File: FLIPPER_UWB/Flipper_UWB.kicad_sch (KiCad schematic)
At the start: 13 parts, among them IC1 DWM1000, J1 Conn_01x08_Socket, J2 Conn_01x10_Socket

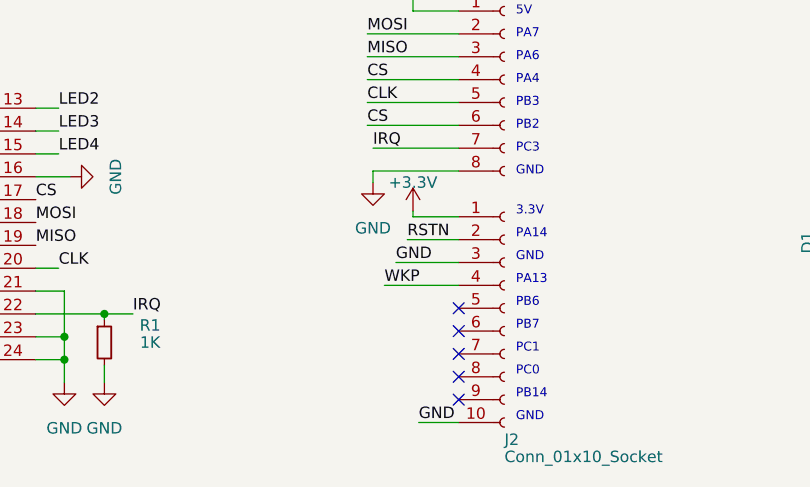
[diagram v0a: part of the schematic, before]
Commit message: Update and correction shield UWB
Update and correction of the Flipper Zero UWB shield.
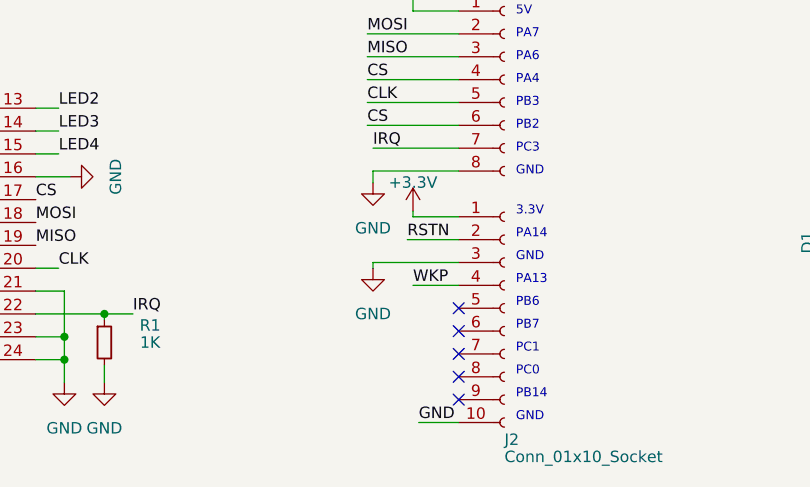
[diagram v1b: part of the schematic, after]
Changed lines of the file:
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@@
-    (stroke (width 0) (type default))
-  )
-  (wire (pts (xy 131.445 56.515) (xy 138.43 56.515))
     (stroke (width 0) (type default))
   )
@@
     (stroke (width 0) (type default))
   )
+  (wire (pts (xy 133.35 59.055) (xy 138.43 59.055))
+    (stroke (width 0) (type default))
+  )
   (wire (pts (xy 212.09 62.23) (xy 212.09 56.515))
     (stroke (width 0) (type default))
@@
     (stroke (width 0) (type default))
   )
+  (wire (pts (xy 128.905 56.515) (xy 138.43 56.515))
+    (stroke (width 0) (type default))
+  )
   (wire (pts (xy 133.35 51.435) (xy 133.35 50.8))
     (stroke (width 0) (type default))
@@
     (stroke (width 0) (type default))
   )
-  (wire (pts (xy 130.175 59.055) (xy 138.43 59.055))
-    (stroke (width 0) (type default))
-  )
   (wire (pts (xy 27.94 57.15) (xy 27.94 58.42))
     (stroke (width 0) (type default))
@@
     (stroke (width 0) (type default))
   )
+  (wire (pts (xy 128.905 56.515) (xy 128.905 57.15))
+    (stroke (width 0) (type default))
+  )
   (wire (pts (xy 21.59 54.61) (xy 33.02 54.61))
     (stroke (width 0) (type default))
@@
     (effects (font (size 1.27 1.27)) (justify left bottom))
   )
-  (label "WKP" (at 130.175 59.055 0) (fields_autoplaced)
+  (label "WKP" (at 133.35 59.055 0) (fields_autoplaced)
     (effects (font (size 1.27 1.27)) (justify left bottom))
   )
@@
     (effects (font (size 1.27 1.27)) (justify left bottom))
   )
-  (label "GND" (at 131.445 56.515 0) (fields_autoplaced)
-    (effects (font (size 1.27 1.27)) (justify left bottom))
-  )
   (label "LED4" (at 93.98 44.45 0) (fields_autoplaced)
     (effects (font (size 1.27 1.27)) (justify left bottom))
@@
     (pin "2")
     (instances
-      (project "Flipper"
+      (project "Flipper_UWB"
         (path "/250e14ef-3436-4bf2-8d4e-c0bb14da8bba"
           (reference "D3") (unit 1)
@@
     (pin "1")
     (instances
-      (project "Flipper"
+      (project "Flipper_UWB"
         (path "/250e14ef-3436-4bf2-8d4e-c0bb14da8bba"
           (reference "#PWR03") (unit 1)
@@
     (pin "2")
     (instances
-      (project "Flipper"
+      (project "Flipper_UWB"
         (path "/250e14ef-3436-4bf2-8d4e-c0bb14da8bba"
           (reference "D4") (unit 1)
@@
     (pin "1")
     (instances
-      (project "Flipper"
+      (project "Flipper_UWB"
         (path "/250e14ef-3436-4bf2-8d4e-c0bb14da8bba"
           (reference "#PWR05") (unit 1)
@@
     (pin "2")
     (instances
-      (project "Flipper"
+      (project "Flipper_UWB"
         (path "/250e14ef-3436-4bf2-8d4e-c0bb14da8bba"
           (reference "R1") (unit 1)
@@
     (pin "2")
     (instances
-      (project "Flipper"
+      (project "Flipper_UWB"
         (path "/250e14ef-3436-4bf2-8d4e-c0bb14da8bba"
           (reference "R2") (unit 1)
@@
     (pin "1")
     (instances
-      (project "Flipper"
+      (project "Flipper_UWB"
         (path "/250e14ef-3436-4bf2-8d4e-c0bb14da8bba"
           (reference "#PWR06") (unit 1)
@@
     (pin "8")
     (instances
-      (project "Flipper"
+      (project "Flipper_UWB"
         (path "/250e14ef-3436-4bf2-8d4e-c0bb14da8bba"
           (reference "J1") (unit 1)
@@
     (pin "1")
     (instances
-      (project "Flipper"
+      (project "Flipper_UWB"
         (path "/250e14ef-3436-4bf2-8d4e-c0bb14da8bba"
           (reference "#PWR09") (unit 1)
@@
     (pin "2")
     (instances
-      (project "Flipper"
+      (project "Flipper_UWB"
         (path "/250e14ef-3436-4bf2-8d4e-c0bb14da8bba"
           (reference "R4") (unit 1)
@@
     (pin "1")
     (instances
-      (project "Flipper"
+      (project "Flipper_UWB"
         (path "/250e14ef-3436-4bf2-8d4e-c0bb14da8bba"
           (reference "#PWR010") (unit 1)
@@
     (pin "2")
     (instances
-      (project "Flipper"
+      (project "Flipper_UWB"
         (path "/250e14ef-3436-4bf2-8d4e-c0bb14da8bba"
           (reference "R3") (unit 1)
@@
     (pin "2")
     (instances
-      (project "Flipper"
+      (project "Flipper_UWB"
         (path "/250e14ef-3436-4bf2-8d4e-c0bb14da8bba"
           (reference "D2") (unit 1)
@@
     (pin "2")
     (instances
-      (project "Flipper"
+      (project "Flipper_UWB"
         (path "/250e14ef-3436-4bf2-8d4e-c0bb14da8bba"
           (reference "R5") (unit 1)
@@
     (pin "1")
     (instances
-      (project "Flipper"
+      (project "Flipper_UWB"
         (path "/250e14ef-3436-4bf2-8d4e-c0bb14da8bba"
           (reference "#PWR02") (unit 1)
@@
     (pin "9")
     (instances
-      (project "Flipper"
+      (project "Flipper_UWB"
         (path "/250e14ef-3436-4bf2-8d4e-c0bb14da8bba"
           (reference "J2") (unit 1)
@@
     (pin "1")
     (instances
-      (project "Flipper"
+      (project "Flipper_UWB"
         (path "/250e14ef-3436-4bf2-8d4e-c0bb14da8bba"
           (reference "#PWR04") (unit 1)
@@
     (pin "2")
     (instances
-      (project "Flipper"
+      (project "Flipper_UWB"
         (path "/250e14ef-3436-4bf2-8d4e-c0bb14da8bba"
           (reference "D1") (unit 1)
@@
     (pin "9")
     (instances
-      (project "Flipper"
+      (project "Flipper_UWB"
         (path "/250e14ef-3436-4bf2-8d4e-c0bb14da8bba"
           (reference "IC1") (unit 1)
@@
     )
   )
+  (symbol (lib_id "power:GND") (at 128.905 57.15 0) (unit 1)
+    (in_bom yes) (on_board yes) (dnp no) (fields_autoplaced)
+    (property "Reference" "#PWR011" (at 128.905 63.5 0)
+      (effects (font (size 1.27 1.27)) hide)
+    )
+    (property "Value" "GND" (at 128.905 62.23 0)
+      (effects (font (size 1.27 1.27)))
+    )
+    (property "Footprint" "" (at 128.905 57.15 0)
+      (effects (font (size 1.27 1.27)) hide)
+    )
+    (property "Datasheet" "" (at 128.905 57.15 0)
+      (effects (font (size 1.27 1.27)) hide)
+    )
+    (pin "1")
+    (instances
+      (project "Flipper_UWB"
+        (path "/250e14ef-3436-4bf2-8d4e-c0bb14da8bba"
+          (reference "#PWR011") (unit 1)
+        )
+      )
+    )
+  )
   (symbol (lib_id "power:GND") (at 21.59 63.5 0) (unit 1)
     (in_bom yes) (on_board yes) (dnp no) (fields_autoplaced)
@@
     (pin "1")
     (instances
-      (project "Flipper"
+      (project "Flipper_UWB"
         (path "/250e14ef-3436-4bf2-8d4e-c0bb14da8bba"
           (reference "#PWR08") (unit 1)
@@
     (pin "1")
     (instances
-      (project "Flipper"
+      (project "Flipper_UWB"
         (path "/250e14ef-3436-4bf2-8d4e-c0bb14da8bba"
           (reference "#PWR07") (unit 1)
@@
     (pin "2")
     (instances
-      (project "Flipper"
+      (project "Flipper_UWB"
         (path "/250e14ef-3436-4bf2-8d4e-c0bb14da8bba"
           (reference "C1") (unit 1)
@@
     (pin "1")
     (instances
-      (project "Flipper"
+      (project "Flipper_UWB"
         (path "/250e14ef-3436-4bf2-8d4e-c0bb14da8bba"
           (reference "#PWR01") (unit 1)

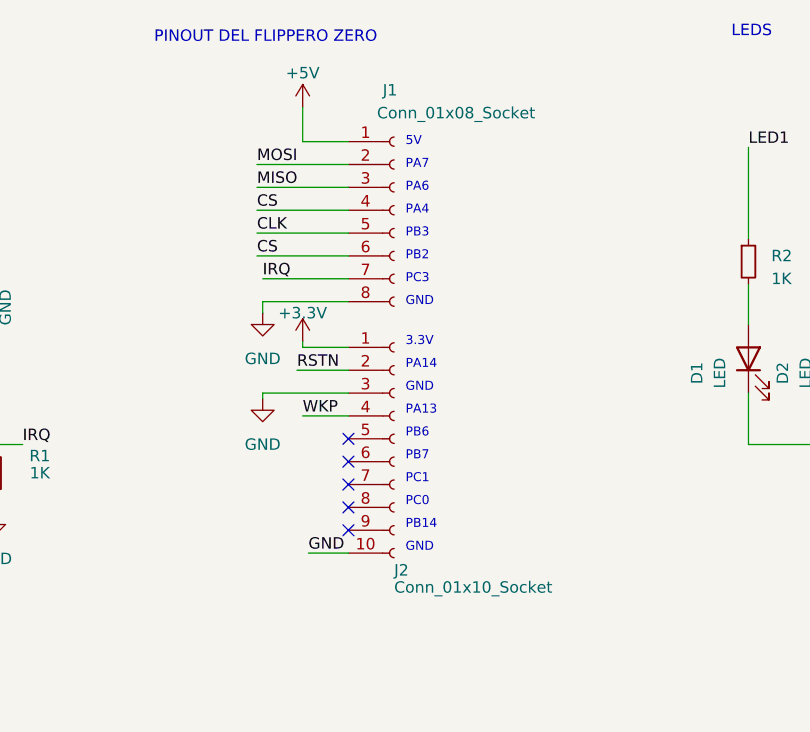
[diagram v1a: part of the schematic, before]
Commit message: Correction of the PCB and the schematic
Correction of the PCB and the schematic of the UBW shield for the FlipperZero
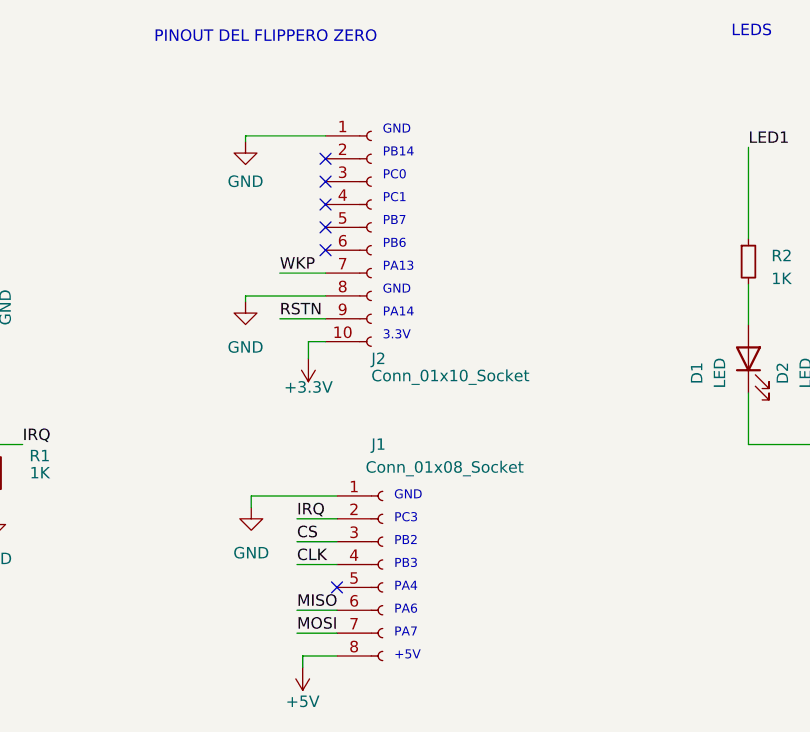
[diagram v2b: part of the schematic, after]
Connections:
- net +3.3V: now also J2.10 (Pin_10); no longer J2.1 (Pin_1)
- net +5V: now also J1.8 (Pin_8); no longer J1.1 (Pin_1)
- net CLK: now also J1.4 (Pin_4); no longer J1.5 (Pin_5)
- net CS: now also J1.3 (Pin_3); no longer J1.4 (Pin_4), J1.6 (Pin_6)
- net GND: now also J1.1 (Pin_1), J2.1 (Pin_1), J2.8 (Pin_8); no longer J1.8 (Pin_8), J2.10 (Pin_10), J2.3 (Pin_3)
- net IRQ: now also J1.2 (Pin_2); no longer J1.7 (Pin_7)
- net MISO: now also J1.6 (Pin_6); no longer J1.3 (Pin_3)
- net MOSI: now also J1.7 (Pin_7); no longer J1.2 (Pin_2)
- net RSTN: now also J2.9 (Pin_9); no longer J2.2 (Pin_2)
- net WKP: now also J2.7 (Pin_7); no longer J2.4 (Pin_4)
- no-connect marks 10 -> 11
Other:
- note added: "+5V"
- note removed: "5V"
- moved on the sheet: J1, J2

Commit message: Update PCB shield UWB
Update PCB shield UWB
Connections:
- net CS: now also J1.5 (Pin_5); no longer J1.3 (Pin_3)
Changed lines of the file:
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@@
   (junction (at 192.405 62.23) (diameter 0) (color 0 0 0 0)
   )
-  (no_connect (at 137.16 78.105))
+  (no_connect (at 137.16 73.025))
   (no_connect (at 33.02 62.23))
   (no_connect (at 135.89 33.02))
@@
     (stroke (width 0) (type default))
   )
+  (wire (pts (xy 132.715 78.105) (xy 137.16 78.105))
+    (stroke (width 0) (type default))
+  )
   (wire (pts (xy 94.615 67.31) (xy 94.615 69.85))
     (stroke (width 0) (type default))
@@
     (stroke (width 0) (type default))
   )
-  (wire (pts (xy 132.715 73.025) (xy 137.16 73.025))
-    (stroke (width 0) (type default))
-  )
   (wire (pts (xy 127 27.94) (xy 127 28.575))
     (stroke (width 0) (type default))
@@
     (effects (font (size 1.27 1.27)) (justify left bottom))
   )
-  (label "CS" (at 132.715 73.025 0) (fields_autoplaced)
-    (effects (font (size 1.27 1.27)) (justify left bottom))
-  )
+  (label "CS" (at 132.715 78.105 0) (fields_autoplaced)
+    (effects (font (size 1.27 1.27)) (justify left bottom))
+  )

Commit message: Update shield UWB
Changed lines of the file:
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@@
+    (stroke (width 0) (type default))
+  )
+  (wire (pts (xy 120.015 53.975) (xy 133.985 53.975))
     (stroke (width 0) (type default))
   )
@@
     (stroke (width 0) (type default))
   )
-  (wire (pts (xy 133.985 50.8) (xy 133.985 52.705))
-    (stroke (width 0) (type default))
-  )
   (wire (pts (xy 132.715 75.565) (xy 137.16 75.565))
     (stroke (width 0) (type default))
@@
     (stroke (width 0) (type default))
   )
-  (wire (pts (xy 127 45.72) (xy 135.89 45.72))
+  (wire (pts (xy 133.985 50.8) (xy 133.985 53.975))
+    (stroke (width 0) (type default))
+  )
+  (wire (pts (xy 125.095 45.72) (xy 135.89 45.72))
     (stroke (width 0) (type default))
   )
@@
     (stroke (width 0) (type default))
   )
+  (wire (pts (xy 129.54 85.725) (xy 129.54 85.09))
+    (stroke (width 0) (type default))
+  )
   (wire (pts (xy 212.09 44.45) (xy 212.09 48.895))
     (stroke (width 0) (type default))
@@
     (stroke (width 0) (type default))
   )
-  (wire (pts (xy 133.35 85.725) (xy 133.35 86.995))
-    (stroke (width 0) (type default))
-  )
   (wire (pts (xy 182.88 62.23) (xy 192.405 62.23))
     (stroke (width 0) (type default))
@@
     (stroke (width 0) (type default))
   )
-  (wire (pts (xy 91.44 46.99) (xy 95.25 46.99))
+  (wire (pts (xy 91.44 46.99) (xy 100.965 46.99))
     (stroke (width 0) (type default))
   )
@@
     (stroke (width 0) (type default))
   )
-  (wire (pts (xy 127 45.72) (xy 127 46.355))
+  (wire (pts (xy 100.965 47.625) (xy 100.965 46.99))
+    (stroke (width 0) (type default))
+  )
+  (wire (pts (xy 125.095 45.72) (xy 125.095 46.355))
     (stroke (width 0) (type default))
   )
@@
     (stroke (width 0) (type default))
   )
-  (wire (pts (xy 137.16 85.725) (xy 133.35 85.725))
+  (wire (pts (xy 129.54 85.725) (xy 137.16 85.725))
     (stroke (width 0) (type default))
   )
@@
       (effects (font (size 1.27 1.27)) hide)
     )
+    (property "DNP" "" (at 201.93 52.705 0)
+      (effects (font (size 1.27 1.27)) hide)
+    )
     (pin "1")
     (pin "2")
@@
       (effects (font (size 1.27 1.27)) hide)
     )
+    (property "DNP" "" (at 212.09 52.705 0)
+      (effects (font (size 1.27 1.27)) hide)
+    )
     (pin "1")
     (pin "2")
@@
     )
   )
-  (symbol (lib_id "power:GND") (at 95.25 46.99 90) (mirror x) (unit 1)
+  (symbol (lib_id "power:GND") (at 100.965 47.625 0) (mirror y) (unit 1)
     (in_bom yes) (on_board yes) (dnp no)
-    (property "Reference" "#PWR05" (at 101.6 46.99 0)
-      (effects (font (size 1.27 1.27)) hide)
-    )
-    (property "Value" "GND" (at 100.33 46.99 0)
-      (effects (font (size 1.27 1.27)))
-    )
-    (property "Footprint" "" (at 95.25 46.99 0)
-      (effects (font (size 1.27 1.27)) hide)
-    )
-    (property "Datasheet" "" (at 95.25 46.99 0)
+    (property "Reference" "#PWR05" (at 100.965 53.975 0)
+      (effects (font (size 1.27 1.27)) hide)
+    )
+    (property "Value" "GND" (at 100.965 52.705 0)
+      (effects (font (size 1.27 1.27)))
+    )
+    (property "Footprint" "" (at 100.965 47.625 0)
+      (effects (font (size 1.27 1.27)) hide)
+    )
+    (property "Datasheet" "" (at 100.965 47.625 0)
       (effects (font (size 1.27 1.27)) hide)
     )
@@
       (effects (font (size 1.27 1.27)) hide)
     )
+    (property "DNP" "" (at 99.06 65.405 0)
+      (effects (font (size 1.27 1.27)) hide)
+    )
     (pin "1")
     (pin "2")
@@
     )
     (property "manf#" "0805W8J0102T5E" (at 182.88 41.91 0)
+      (effects (font (size 1.27 1.27)) hide)
+    )
+    (property "DNP" "" (at 182.88 41.91 0)
       (effects (font (size 1.27 1.27)) hide)
     )
@@
     )
     (property "manf#" "PZ2.54-1*20-WZ" (at 142.24 75.565 0)
+      (effects (font (size 1.27 1.27)) hide)
+    )
+    (property "DNP" "" (at 142.24 75.565 0)
       (effects (font (size 1.27 1.27)) hide)
     )
@@
       (effects (font (size 1.27 1.27)) hide)
     )
+    (property "DNP" "" (at 201.93 41.91 0)
+      (effects (font (size 1.27 1.27)) hide)
+    )
     (pin "1")
     (pin "2")
@@
     )
   )
-  (symbol (lib_id "power:+3.3V") (at 133.985 52.705 180) (unit 1)
-    (in_bom yes) (on_board yes) (dnp no) (fields_autoplaced)
-    (property "Reference" "#PWR010" (at 133.985 48.895 0)
-      (effects (font (size 1.27 1.27)) hide)
-    )
-    (property "Value" "+3.3V" (at 133.985 55.88 0)
-      (effects (font (size 1.27 1.27)))
-    )
-    (property "Footprint" "" (at 133.985 52.705 0)
-      (effects (font (size 1.27 1.27)) hide)
-    )
-    (property "Datasheet" "" (at 133.985 52.705 0)
+  (symbol (lib_id "power:+3.3V") (at 120.015 53.975 0) (unit 1)
+    (in_bom yes) (on_board yes) (dnp no) (fields_autoplaced)
+    (property "Reference" "#PWR010" (at 120.015 57.785 0)
+      (effects (font (size 1.27 1.27)) hide)
+    )
+    (property "Value" "+3.3V" (at 120.015 50.8 0)
+      (effects (font (size 1.27 1.27)))
+    )
+    (property "Footprint" "" (at 120.015 53.975 0)
+      (effects (font (size 1.27 1.27)) hide)
+    )
+    (property "Datasheet" "" (at 120.015 53.975 0)
       (effects (font (size 1.27 1.27)) hide)
     )
@@
     )
     (property "manf#" "0805W8J0102T5E" (at 192.405 41.91 0)
+      (effects (font (size 1.27 1.27)) hide)
+    )
+    (property "DNP" "" (at 192.405 41.91 0)
       (effects (font (size 1.27 1.27)) hide)
     )
@@
       (effects (font (size 1.27 1.27)) hide)
     )
+    (property "DNP" "" (at 192.405 52.705 0)
+      (effects (font (size 1.27 1.27)) hide)
+    )
     (pin "1")
     (pin "2")
@@
     )
     (property "manf#" "0805W8J0102T5E" (at 212.09 41.91 0)
+      (effects (font (size 1.27 1.27)) hide)
+    )
+    (property "DNP" "" (at 212.09 41.91 0)
       (effects (font (size 1.27 1.27)) hide)
     )
@@
     )
     (property "manf#" "PZ2.54-1*20-WZ" (at 140.97 38.1 0)
+      (effects (font (size 1.27 1.27)) hide)
+    )
+    (property "DNP" "" (at 140.97 38.1 0)
       (effects (font (size 1.27 1.27)) hide)
     )
@@
     )
   )
-  (symbol (lib_id "power:+5V") (at 133.35 86.995 180) (unit 1)
-    (in_bom yes) (on_board yes) (dnp no) (fields_autoplaced)
-    (property "Reference" "#PWR04" (at 133.35 83.185 0)
-      (effects (font (size 1.27 1.27)) hide)
-    )
-    (property "Value" "+5V" (at 133.35 90.805 0)
-      (effects (font (size 1.27 1.27)))
-    )
-    (property "Footprint" "" (at 133.35 86.995 0)
-      (effects (font (size 1.27 1.27)) hide)
-    )
-    (property "Datasheet" "" (at 133.35 86.995 0)
+  (symbol (lib_id "power:+5V") (at 129.54 85.09 0) (unit 1)
+    (in_bom yes) (on_board yes) (dnp no)
+    (property "Reference" "#PWR04" (at 129.54 88.9 0)
+      (effects (font (size 1.27 1.27)) hide)
+    )
+    (property "Value" "+5V" (at 129.54 80.645 0)
+      (effects (font (size 1.27 1.27)))
+    )
+    (property "Footprint" "" (at 129.54 85.09 0)
+      (effects (font (size 1.27 1.27)) hide)
+    )
+    (property "Datasheet" "" (at 129.54 85.09 0)
       (effects (font (size 1.27 1.27)) hide)
     )
@@
     )
     (property "manf#" "ORH-G35A" (at 182.88 52.705 0)
+      (effects (font (size 1.27 1.27)) hide)
+    )
+    (property "DNP" "" (at 182.88 52.705 0)
       (effects (font (size 1.27 1.27)) hide)
     )
@@
     )
     (property "manf#" "772-DWM1000" (at 33.02 39.37 0)
+      (effects (font (size 1.27 1.27)) hide)
+    )
+    (property "DNP" "" (at 33.02 39.37 0)
       (effects (font (size 1.27 1.27)) hide)
     )
@@
     )
   )
-  (symbol (lib_id "power:GND") (at 127 46.355 0) (unit 1)
-    (in_bom yes) (on_board yes) (dnp no) (fields_autoplaced)
-    (property "Reference" "#PWR011" (at 127 52.705 0)
-      (effects (font (size 1.27 1.27)) hide)
-    )
-    (property "Value" "GND" (at 127 51.435 0)
-      (effects (font (size 1.27 1.27)))
-    )
-    (property "Footprint" "" (at 127 46.355 0)
-      (effects (font (size 1.27 1.27)) hide)
-    )
-    (property "Datasheet" "" (at 127 46.355 0)
+  (symbol (lib_id "power:GND") (at 125.095 46.355 0) (unit 1)
+    (in_bom yes) (on_board yes) (dnp no)
+    (property "Reference" "#PWR011" (at 125.095 52.705 0)
+      (effects (font (size 1.27 1.27)) hide)
+    )
+    (property "Value" "GND" (at 122.555 46.355 0)
+      (effects (font (size 1.27 1.27)))
+    )
+    (property "Footprint" "" (at 125.095 46.355 0)
+      (effects (font (size 1.27 1.27)) hide)
+    )
+    (property "Datasheet" "" (at 125.095 46.355 0)
       (effects (font (size 1.27 1.27)) hide)
     )
@@
       (effects (font (size 1.27 1.27)) hide)
     )
+    (property "DNP" "" (at 21.59 58.42 0)
+      (effects (font (size 1.27 1.27)) hide)
+    )

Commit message: Add_HTML
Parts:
- C1: Manufacturer_Name KYOCERA AVX -> (none); Manufacturer_Part_Number TLCR107M006RTA -> (none); Mouser Part Number 581-TLCR107M006RTA -> (none); Mouser Price/Stock https://www.mouser.mx/ProductDetail/KYOCERA-AVX/TLCR107M006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 -> (none); manf# 581-TLCR107M006RTA -> TLCR107M006RTA
- D1, D2: LCSC Part Number C205442 -> (none); LCSC Price/Stock https://www.lcsc.com/product-detail/Light-Emitting-Diodes-L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 -> (none); Manufacturer_Name Orient -> (none); Manufacturer_Part_Number ORH-G35A -> (none)
- D3: LCSC Part Number C84261 -> (none); LCSC Price/Stock https://www.lcsc.com/product-detail/Light-Emitting-Diodes-s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 -> (none); Manufacturer_Name Foshan NationStar Optoelectronics -> (none); Manufacturer_Part_Number NCD0805Y1 -> (none)
- D4: LCSC Part Number C130114 -> (none); LCSC Price/Stock https://www.lcsc.com/product-detail/Light-Emitting-Diodes-L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 -> (none); Manufacturer_Name ARKLED -> (none); Manufacturer_Part_Number D-R080508L3-KS2 -> (none)
- IC1: Height 3.15 -> (none); Manufacturer_Name Qorvo -> (none); Manufacturer_Part_Number DWM1000 -> (none); Mouser Part Number 772-DWM1000 -> (none); Mouser Price/Stock https://www.mouser.co.uk/ProductDetail/Qorvo/DWM1000?qs=TiO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 -> (none)
- J1, J2: LCSC# C5360907 -> (none); Proveedor LCSC -> Mouser; manf# PZ2.54-1*20-WZ -> M20-9961045
- R1, R2, R3, R4, R5: LCSC Part Number C25623 -> (none); LCSC Price/Stock https://www.lcsc.com/product-detail/Chip-Resistor-Surface-M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 -> (none); Manufacturer_Name Uniroyal Elec -> (none); Manufacturer_Part_Number 0805W8J0102T5E -> (none)
